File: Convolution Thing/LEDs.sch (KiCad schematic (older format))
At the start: 6 parts

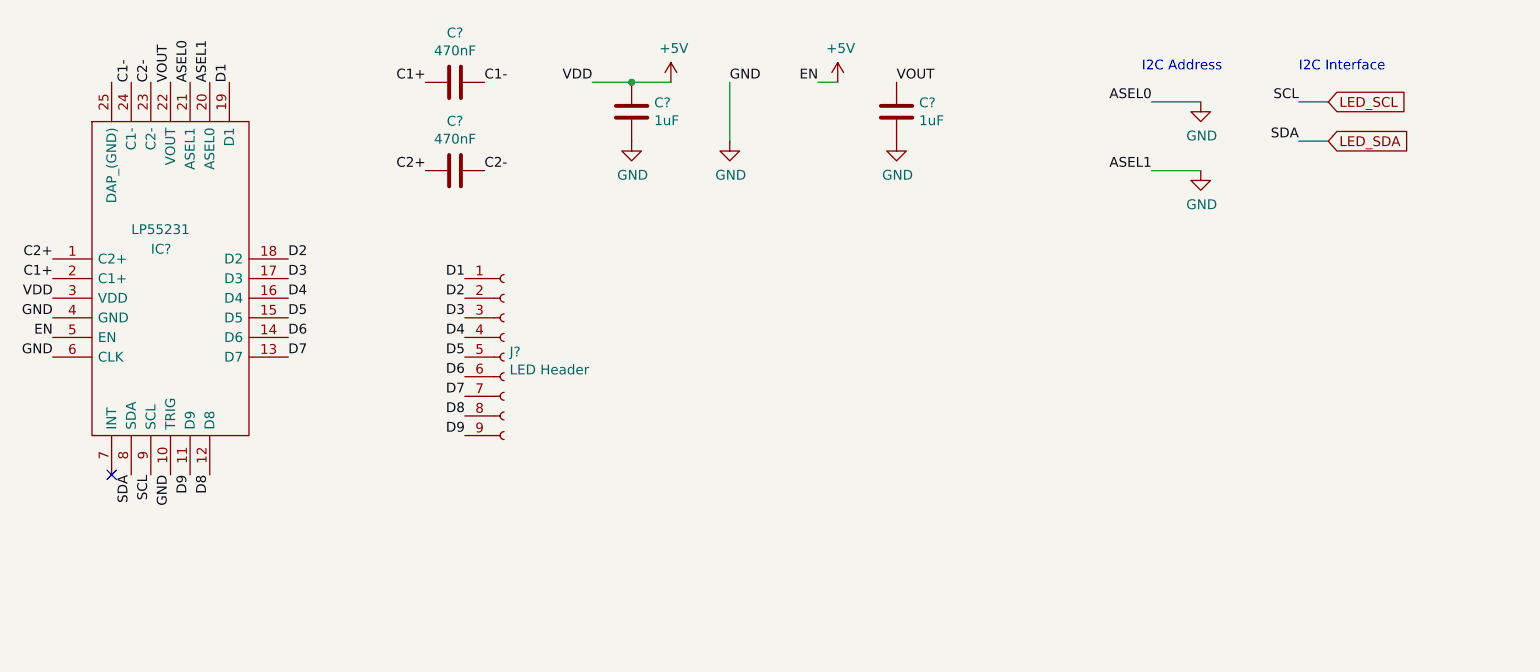
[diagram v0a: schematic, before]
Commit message: Added gate inputs and CM4 / display sockets, made CV inputs 100k, lots of smaller changes. First iteration of schematic now done.
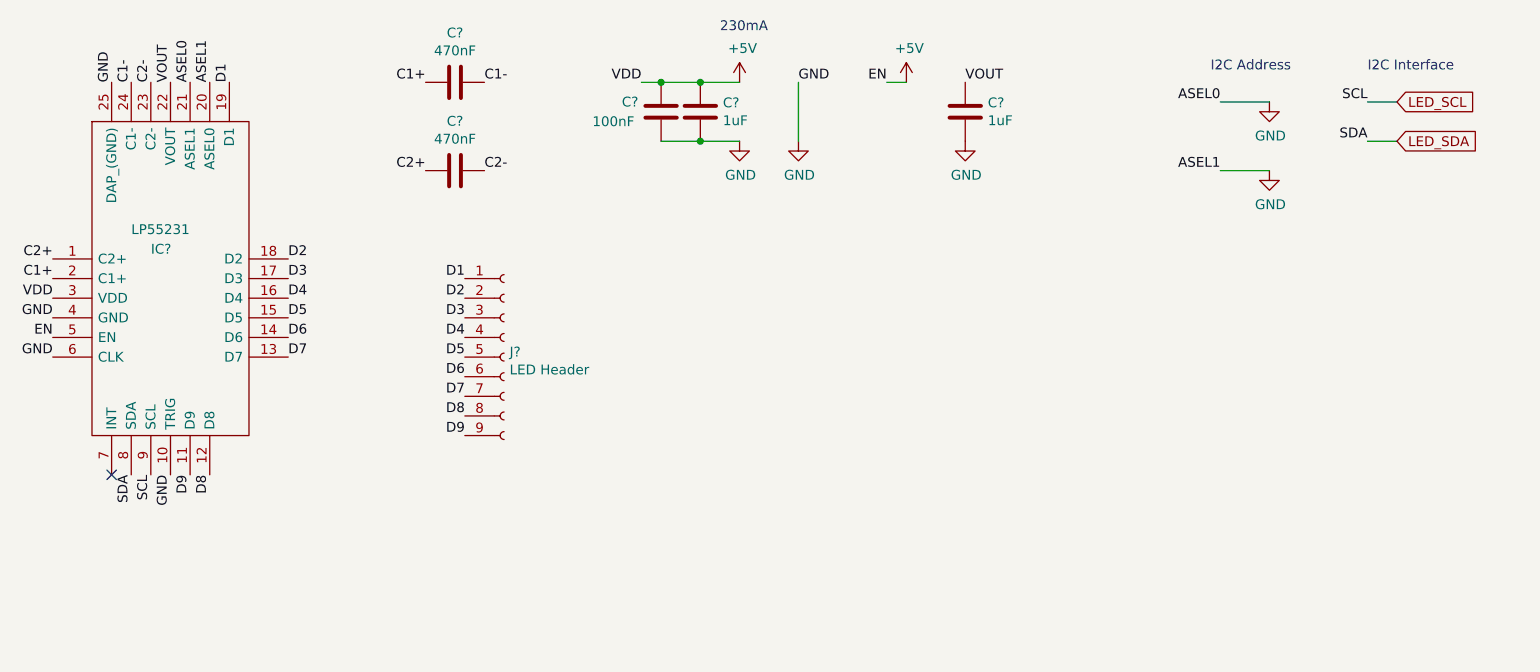
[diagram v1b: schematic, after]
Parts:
- added C?: 100nF, symbol Device:C
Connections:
- net +5V: now also C?.1
- net GND: now also IC?.25 (DAP_(GND)), C?.2
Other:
- note added: "230mA"
- moved on the sheet: C?
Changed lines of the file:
@@
 $Descr A4 11693 8268
 encoding utf-8
-Sheet 10 11
+Sheet 10 13
 Title ""
 Date ""
@@
 L power:+5V #PWR?
 U 1 1 611E96FD
-P 4350 1000
-F 0 "#PWR?" H 4350 850 50  0001 C CNN
-F 1 "+5V" H 4365 1173 50  0000 C CNN
-F 2 "" H 4350 1000 50  0001 C CNN
-F 3 "" H 4350 1000 50  0001 C CNN
-	1    4350 1000
-	1    0    0    -1
-$EndComp
-Text Label 3950 1000 2    50   ~ 0
+P 4700 1000
+F 0 "#PWR?" H 4700 850 50  0001 C CNN
+F 1 "+5V" H 4715 1173 50  0000 C CNN
+F 2 "" H 4700 1000 50  0001 C CNN
+F 3 "" H 4700 1000 50  0001 C CNN
+	1    4700 1000
+	1    0    0    -1
+$EndComp
+Text Label 4200 1000 2    50   ~ 0
 VDD
 $Comp
 L Device:C C?
 U 1 1 611EA9E5
-P 4150 1150
-F 0 "C?" H 4265 1196 50  0000 L CNN
-F 1 "1uF" H 4265 1105 50  0000 L CNN
-F 2 "" H 4188 1000 50  0001 C CNN
-F 3 "~" H 4150 1150 50  0001 C CNN
-	1    4150 1150
-	1    0    0    -1
-$EndComp
-Wire Wire Line
-	4350 1000 4150 1000
-Wire Wire Line
-	4150 1000 3950 1000
-Connection ~ 4150 1000
+P 4500 1150
+F 0 "C?" H 4615 1196 50  0000 L CNN
+F 1 "1uF" H 4615 1105 50  0000 L CNN
+F 2 "" H 4538 1000 50  0001 C CNN
+F 3 "~" H 4500 1150 50  0001 C CNN
+	1    4500 1150
+	1    0    0    -1
+$EndComp
+Wire Wire Line
+	4700 1000 4500 1000
+Wire Wire Line
+	4500 1000 4300 1000
+Connection ~ 4500 1000
 $Comp
 L power:GND #PWR?
 U 1 1 611EAE26
-P 4150 1300
-F 0 "#PWR?" H 4150 1050 50  0001 C CNN
-F 1 "GND" H 4155 1127 50  0000 C CNN
-F 2 "" H 4150 1300 50  0001 C CNN
-F 3 "" H 4150 1300 50  0001 C CNN
-	1    4150 1300
-	1    0    0    -1
-$EndComp
-Text Label 4650 1000 0    50   ~ 0
+P 4700 1300
+F 0 "#PWR?" H 4700 1050 50  0001 C CNN
+F 1 "GND" H 4705 1127 50  0000 C CNN
+F 2 "" H 4700 1300 50  0001 C CNN
+F 3 "" H 4700 1300 50  0001 C CNN
+	1    4700 1300
+	1    0    0    -1
+$EndComp
+Text Label 5000 1000 0    50   ~ 0
 GND
 $Comp
 L power:GND #PWR?
 U 1 1 611EC0F9
-P 4650 1300
-F 0 "#PWR?" H 4650 1050 50  0001 C CNN
-F 1 "GND" H 4655 1127 50  0000 C CNN
-F 2 "" H 4650 1300 50  0001 C CNN
-F 3 "" H 4650 1300 50  0001 C CNN
-	1    4650 1300
-	1    0    0    -1
-$EndComp
-Wire Wire Line
-	4650 1300 4650 1000
+P 5000 1300
+F 0 "#PWR?" H 5000 1050 50  0001 C CNN
+F 1 "GND" H 5005 1127 50  0000 C CNN
+F 2 "" H 5000 1300 50  0001 C CNN
+F 3 "" H 5000 1300 50  0001 C CNN
+	1    5000 1300
+	1    0    0    -1
+$EndComp
+Wire Wire Line
+	5000 1300 5000 1000
 Text Label 1200 2400 2    50   ~ 0
 GND
 Text Label 1200 2300 2    50   ~ 0
 EN
-Text Label 5100 1000 2    50   ~ 0
+Text Label 5450 1000 2    50   ~ 0
 EN
 $Comp
 L power:+5V #PWR?
 U 1 1 611EF36E
-P 5200 1000
-F 0 "#PWR?" H 5200 850 50  0001 C CNN
-F 1 "+5V" H 5215 1173 50  0000 C CNN
-F 2 "" H 5200 1000 50  0001 C CNN
-F 3 "" H 5200 1000 50  0001 C CNN
-	1    5200 1000
-	1    0    0    -1
-$EndComp
-Wire Wire Line
-	5200 1000 5100 1000
+P 5550 1000
+F 0 "#PWR?" H 5550 850 50  0001 C CNN
+F 1 "+5V" H 5565 1173 50  0000 C CNN
+F 2 "" H 5550 1000 50  0001 C CNN
+F 3 "" H 5550 1000 50  0001 C CNN
+	1    5550 1000
+	1    0    0    -1
+$EndComp
+Wire Wire Line
+	5550 1000 5450 1000
 NoConn ~ 1500 3000
 Text Label 1600 3000 3    50   ~ 0
@@
 Text Label 1700 3000 3    50   ~ 0
 SCL
-Text Notes 6750 950  0    50   ~ 0
+Text Notes 7100 950  0    50   ~ 0
 I2C Address
 Text Label 1900 1000 1    50   ~ 0
@@
 Text Label 2000 1000 1    50   ~ 0
 ASEL1
-Text Label 6800 1100 2    50   ~ 0
+Text Label 7150 1100 2    50   ~ 0
 ASEL0
-Text Label 6800 1450 2    50   ~ 0
+Text Label 7150 1450 2    50   ~ 0
 ASEL1
 $Comp
 L power:GND #PWR?
 U 1 1 611F4B43
-P 7050 1100
-F 0 "#PWR?" H 7050 850 50  0001 C CNN
-F 1 "GND" H 7055 927 50  0000 C CNN
-F 2 "" H 7050 1100 50  0001 C CNN
-F 3 "" H 7050 1100 50  0001 C CNN
-	1    7050 1100
-	1    0    0    -1
-$EndComp
-Wire Wire Line
-	7050 1100 6800 1100
+P 7400 1100
+F 0 "#PWR?" H 7400 850 50  0001 C CNN
+F 1 "GND" H 7405 927 50  0000 C CNN
+F 2 "" H 7400 1100 50  0001 C CNN
+F 3 "" H 7400 1100 50  0001 C CNN
+	1    7400 1100
+	1    0    0    -1
+$EndComp
+Wire Wire Line
+	7400 1100 7150 1100
 $Comp
 L power:GND #PWR?
 U 1 1 611F4F3E
-P 7050 1450
-F 0 "#PWR?" H 7050 1200 50  0001 C CNN
-F 1 "GND" H 7055 1277 50  0000 C CNN
-F 2 "" H 7050 1450 50  0001 C CNN
-F 3 "" H 7050 1450 50  0001 C CNN
-	1    7050 1450
-	1    0    0    -1
-$EndComp
-Wire Wire Line
-	7050 1450 6800 1450
-Text Notes 7550 950  0    50   ~ 0
+P 7400 1450
+F 0 "#PWR?" H 7400 1200 50  0001 C CNN
+F 1 "GND" H 7405 1277 50  0000 C CNN
+F 2 "" H 7400 1450 50  0001 C CNN
+F 3 "" H 7400 1450 50  0001 C CNN
+	1    7400 1450
+	1    0    0    -1
+$EndComp
+Wire Wire Line
+	7400 1450 7150 1450
+Text Notes 7900 950  0    50   ~ 0
 I2C Interface
-Text Label 7550 1100 2    50   ~ 0
+Text Label 7900 1100 2    50   ~ 0
 SCL
-Text Label 7550 1300 2    50   ~ 0
+Text Label 7900 1300 2    50   ~ 0
 SDA
-Text GLabel 7700 1100 2    50   Input ~ 0
+Text GLabel 8050 1100 2    50   Input ~ 0
 LED_SCL
-Text GLabel 7700 1300 2    50   Input ~ 0
+Text GLabel 8050 1300 2    50   Input ~ 0
 LED_SDA
 Wire Wire Line
-	7700 1300 7550 1300
-Wire Wire Line
-	7550 1100 7700 1100
+	8050 1300 7900 1300
+Wire Wire Line
+	7900 1100 8050 1100
 Text Label 1800 3000 3    50   ~ 0
 GND
 Text Label 1800 1000 1    50   ~ 0
 VOUT
-Text Label 5500 1000 0    50   ~ 0
+Text Label 5850 1000 0    50   ~ 0
 VOUT
 $Comp
 L Device:C C?
 U 1 1 611FB309
-P 5500 1150
-F 0 "C?" H 5615 1196 50  0000 L CNN
-F 1 "1uF" H 5615 1105 50  0000 L CNN
-F 2 "" H 5538 1000 50  0001 C CNN
-F 3 "~" H 5500 1150 50  0001 C CNN
-	1    5500 1150
+P 5850 1150
+F 0 "C?" H 5965 1196 50  0000 L CNN
+F 1 "1uF" H 5965 1105 50  0000 L CNN
+F 2 "" H 5888 1000 50  0001 C CNN
+F 3 "~" H 5850 1150 50  0001 C CNN
+	1    5850 1150
 	1    0    0    -1
 $EndComp
@@
 L power:GND #PWR?
 U 1 1 611FB5AF
-P 5500 1300
-F 0 "#PWR?" H 5500 1050 50  0001 C CNN
-F 1 "GND" H 5505 1127 50  0000 C CNN
-F 2 "" H 5500 1300 50  0001 C CNN
-F 3 "" H 5500 1300 50  0001 C CNN
-	1    5500 1300
+P 5850 1300
+F 0 "#PWR?" H 5850 1050 50  0001 C CNN
+F 1 "GND" H 5855 1127 50  0000 C CNN
+F 2 "" H 5850 1300 50  0001 C CNN
+F 3 "" H 5850 1300 50  0001 C CNN
+	1    5850 1300
 	1    0    0    -1
 $EndComp
@@
 Text Label 3300 2800 2    50   ~ 0
 D9
+Text Label 1500 1000 1    50   ~ 0
+GND
+Text Notes 4600 750  0    50   ~ 0
+230mA
+$Comp
+L Device:C C?
+U 1 1 612CC466
+P 4300 1150
+F 0 "C?" H 4100 1200 50  0000 L CNN
+F 1 "100nF" H 3950 1100 50  0000 L CNN
+F 2 "" H 4338 1000 50  0001 C CNN
+F 3 "~" H 4300 1150 50  0001 C CNN
+	1    4300 1150
+	1    0    0    -1
+$EndComp
+Wire Wire Line
+	4200 1000 4300 1000
+Connection ~ 4300 1000
+Wire Wire Line
+	4300 1300 4500 1300
+Wire Wire Line
+	4500 1300 4700 1300
+Connection ~ 4500 1300
 $EndSCHEMATC

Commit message: Fix some issues, add component references
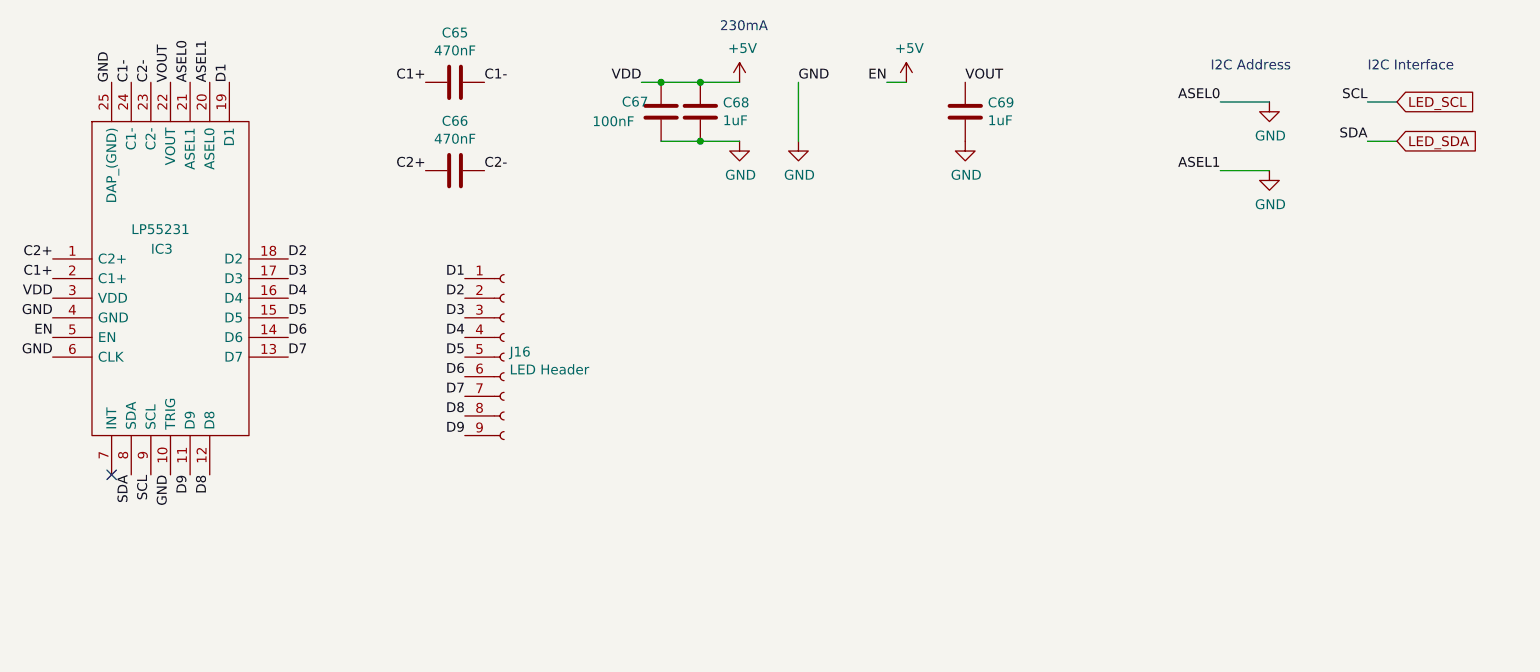
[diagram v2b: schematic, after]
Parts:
- gave numbers to parts that had none: 7
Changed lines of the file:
@@
 $EndDescr
 $Comp
-L SamacSys:LP55231SQE_NOPB IC?
+L SamacSys:LP55231SQE_NOPB IC3
 U 1 1 611DF4B0
 P 1200 1900
-F 0 "IC?" H 1700 1950 50  0000 L CNN
+F 0 "IC3" H 1700 1950 50  0000 L CNN
 F 1 "LP55231" H 1600 2050 50  0000 L CNN
 F 2 "QFN50P400X400X80-25N" H 2250 2600 50  0001 L CNN
@@
 C1+
 $Comp
-L Device:C C?
+L Device:C C65
 U 1 1 611E401F
 P 3250 1000
-F 0 "C?" V 2998 1000 50  0000 C CNN
+F 0 "C65" V 2998 1000 50  0000 C CNN
 F 1 "470nF" V 3089 1000 50  0000 C CNN
 F 2 "" H 3288 850 50  0001 C CNN
@@
 C2+
 $Comp
-L Device:C C?
+L Device:C C66
 U 1 1 611E6D48
 P 3250 1450
-F 0 "C?" V 2998 1450 50  0000 C CNN
+F 0 "C66" V 2998 1450 50  0000 C CNN
 F 1 "470nF" V 3089 1450 50  0000 C CNN
 F 2 "" H 3288 1300 50  0001 C CNN
@@
 C2-
 $Comp
-L power:+5V #PWR?
+L power:+5V #PWR0119
 U 1 1 611E96FD
 P 4700 1000
-F 0 "#PWR?" H 4700 850 50  0001 C CNN
+F 0 "#PWR0119" H 4700 850 50  0001 C CNN
 F 1 "+5V" H 4715 1173 50  0000 C CNN
 F 2 "" H 4700 1000 50  0001 C CNN
@@
 VDD
 $Comp
-L Device:C C?
+L Device:C C68
 U 1 1 611EA9E5
 P 4500 1150
-F 0 "C?" H 4615 1196 50  0000 L CNN
+F 0 "C68" H 4615 1196 50  0000 L CNN
 F 1 "1uF" H 4615 1105 50  0000 L CNN
 F 2 "" H 4538 1000 50  0001 C CNN
@@
 Connection ~ 4500 1000
 $Comp
-L power:GND #PWR?
+L power:GND #PWR0120
 U 1 1 611EAE26
 P 4700 1300
-F 0 "#PWR?" H 4700 1050 50  0001 C CNN
+F 0 "#PWR0120" H 4700 1050 50  0001 C CNN
 F 1 "GND" H 4705 1127 50  0000 C CNN
 F 2 "" H 4700 1300 50  0001 C CNN
@@
 GND
 $Comp
-L power:GND #PWR?
+L power:GND #PWR0121
 U 1 1 611EC0F9
 P 5000 1300
-F 0 "#PWR?" H 5000 1050 50  0001 C CNN
+F 0 "#PWR0121" H 5000 1050 50  0001 C CNN
 F 1 "GND" H 5005 1127 50  0000 C CNN
 F 2 "" H 5000 1300 50  0001 C CNN
@@
 EN
 $Comp
-L power:+5V #PWR?
+L power:+5V #PWR0122
 U 1 1 611EF36E
 P 5550 1000
-F 0 "#PWR?" H 5550 850 50  0001 C CNN
+F 0 "#PWR0122" H 5550 850 50  0001 C CNN
 F 1 "+5V" H 5565 1173 50  0000 C CNN
 F 2 "" H 5550 1000 50  0001 C CNN
@@
 ASEL1
 $Comp
-L power:GND #PWR?
+L power:GND #PWR0124
 U 1 1 611F4B43
 P 7400 1100
-F 0 "#PWR?" H 7400 850 50  0001 C CNN
+F 0 "#PWR0124" H 7400 850 50  0001 C CNN
 F 1 "GND" H 7405 927 50  0000 C CNN
 F 2 "" H 7400 1100 50  0001 C CNN
@@
 	7400 1100 7150 1100
 $Comp
-L power:GND #PWR?
+L power:GND #PWR0125
 U 1 1 611F4F3E
 P 7400 1450
-F 0 "#PWR?" H 7400 1200 50  0001 C CNN
+F 0 "#PWR0125" H 7400 1200 50  0001 C CNN
 F 1 "GND" H 7405 1277 50  0000 C CNN
 F 2 "" H 7400 1450 50  0001 C CNN
@@
 VOUT
 $Comp
-L Device:C C?
+L Device:C C69
 U 1 1 611FB309
 P 5850 1150
-F 0 "C?" H 5965 1196 50  0000 L CNN
+F 0 "C69" H 5965 1196 50  0000 L CNN
 F 1 "1uF" H 5965 1105 50  0000 L CNN
 F 2 "" H 5888 1000 50  0001 C CNN
@@
 $EndComp
 $Comp
-L power:GND #PWR?
+L power:GND #PWR0123
 U 1 1 611FB5AF
 P 5850 1300
-F 0 "#PWR?" H 5850 1050 50  0001 C CNN
+F 0 "#PWR0123" H 5850 1050 50  0001 C CNN
 F 1 "GND" H 5855 1127 50  0000 C CNN
 F 2 "" H 5850 1300 50  0001 C CNN
@@
 D9
 $Comp
-L Connector:Conn_01x09_Female J?
+L Connector:Conn_01x09_Female J16
 U 1 1 611FEF8C
 P 3500 2400
-F 0 "J?" H 3528 2426 50  0000 L CNN
+F 0 "J16" H 3528 2426 50  0000 L CNN
 F 1 "LED Header" H 3528 2335 50  0000 L CNN
 F 2 "" H 3500 2400 50  0001 C CNN
@@
 230mA
 $Comp
-L Device:C C?
+L Device:C C67
 U 1 1 612CC466
 P 4300 1150
-F 0 "C?" H 4100 1200 50  0000 L CNN
+F 0 "C67" H 4100 1200 50  0000 L CNN
 F 1 "100nF" H 3950 1100 50  0000 L CNN
 F 2 "" H 4338 1000 50  0001 C CNN

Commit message: Started footprint assignment
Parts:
- IC3: footprint QFN50P400X400X80-25N -> SamacSys:QFN50P400X400X80-25N
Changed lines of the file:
@@
 F 0 "IC3" H 1700 1950 50  0000 L CNN
 F 1 "LP55231" H 1600 2050 50  0000 L CNN
-F 2 "QFN50P400X400X80-25N" H 2250 2600 50  0001 L CNN
+F 2 "SamacSys:QFN50P400X400X80-25N" H 2250 2600 50  0001 L CNN
 F 3 "" H 2250 2500 50  0001 L CNN
 F 4 "9 Channel RGB / White LED Driver with Internal Program Memory and Integrated Charge Pump - WQFN" H 2250 2400 50  0001 L CNN "Description"

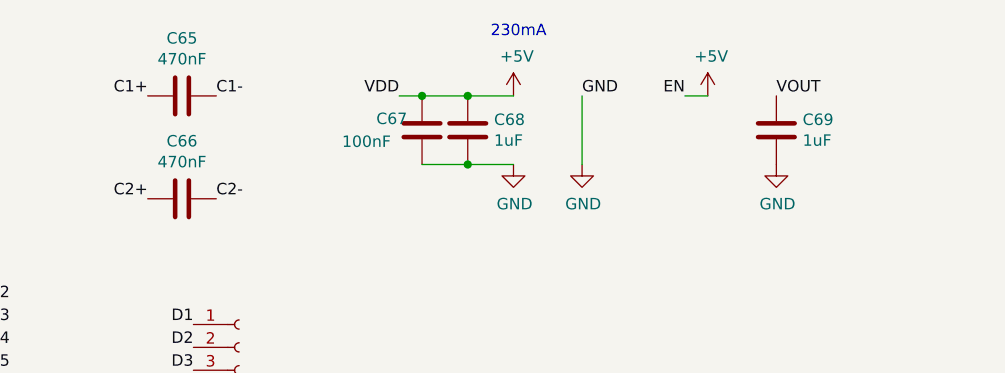
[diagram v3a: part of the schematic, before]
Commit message: Assign all footprints
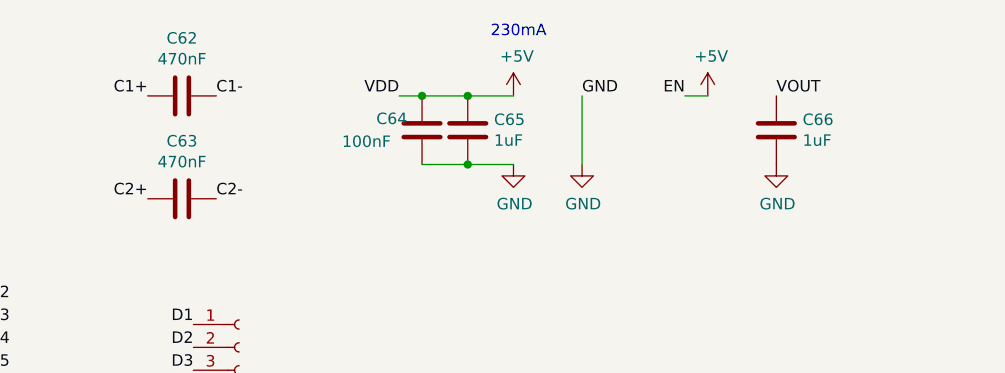
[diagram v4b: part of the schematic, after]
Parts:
- C62: renamed from C65; footprint (none) -> Capacitor_SMD:C_0805_2012Metric
- C63: renamed from C66; footprint (none) -> Capacitor_SMD:C_0805_2012Metric
- C64: renamed from C67; footprint (none) -> Capacitor_SMD:C_0805_2012Metric
- C65: renamed from C68; footprint (none) -> Capacitor_SMD:C_0805_2012Metric
- C66: renamed from C69; footprint (none) -> Capacitor_SMD:C_0805_2012Metric
- J16: footprint (none) -> Connector_PinHeader_2.54mm:PinHeader_1x09_P2.54mm_Vertical
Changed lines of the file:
@@
 C1+
 $Comp
-L Device:C C65
+L Device:C C62
 U 1 1 611E401F
 P 3250 1000
-F 0 "C65" V 2998 1000 50  0000 C CNN
+F 0 "C62" V 2998 1000 50  0000 C CNN
 F 1 "470nF" V 3089 1000 50  0000 C CNN
-F 2 "" H 3288 850 50  0001 C CNN
+F 2 "Capacitor_SMD:C_0805_2012Metric" H 3288 850 50  0001 C CNN
 F 3 "~" H 3250 1000 50  0001 C CNN
 	1    3250 1000
@@
 C2+
 $Comp
-L Device:C C66
+L Device:C C63
 U 1 1 611E6D48
 P 3250 1450
-F 0 "C66" V 2998 1450 50  0000 C CNN
+F 0 "C63" V 2998 1450 50  0000 C CNN
 F 1 "470nF" V 3089 1450 50  0000 C CNN
-F 2 "" H 3288 1300 50  0001 C CNN
+F 2 "Capacitor_SMD:C_0805_2012Metric" H 3288 1300 50  0001 C CNN
 F 3 "~" H 3250 1450 50  0001 C CNN
 	1    3250 1450
@@
 C2-
 $Comp
-L power:+5V #PWR0119
+L power:+5V #PWR0112
 U 1 1 611E96FD
 P 4700 1000
-F 0 "#PWR0119" H 4700 850 50  0001 C CNN
+F 0 "#PWR0112" H 4700 850 50  0001 C CNN
 F 1 "+5V" H 4715 1173 50  0000 C CNN
 F 2 "" H 4700 1000 50  0001 C CNN
@@
 VDD
 $Comp
-L Device:C C68
+L Device:C C65
 U 1 1 611EA9E5
 P 4500 1150
-F 0 "C68" H 4615 1196 50  0000 L CNN
+F 0 "C65" H 4615 1196 50  0000 L CNN
 F 1 "1uF" H 4615 1105 50  0000 L CNN
-F 2 "" H 4538 1000 50  0001 C CNN
+F 2 "Capacitor_SMD:C_0805_2012Metric" H 4538 1000 50  0001 C CNN
 F 3 "~" H 4500 1150 50  0001 C CNN
 	1    4500 1150
@@
 Connection ~ 4500 1000
 $Comp
-L power:GND #PWR0120
+L power:GND #PWR0113
 U 1 1 611EAE26
 P 4700 1300
-F 0 "#PWR0120" H 4700 1050 50  0001 C CNN
+F 0 "#PWR0113" H 4700 1050 50  0001 C CNN
 F 1 "GND" H 4705 1127 50  0000 C CNN
 F 2 "" H 4700 1300 50  0001 C CNN
@@
 GND
 $Comp
-L power:GND #PWR0121
+L power:GND #PWR0114
 U 1 1 611EC0F9
 P 5000 1300
-F 0 "#PWR0121" H 5000 1050 50  0001 C CNN
+F 0 "#PWR0114" H 5000 1050 50  0001 C CNN
 F 1 "GND" H 5005 1127 50  0000 C CNN
 F 2 "" H 5000 1300 50  0001 C CNN
@@
 EN
 $Comp
-L power:+5V #PWR0122
+L power:+5V #PWR0115
 U 1 1 611EF36E
 P 5550 1000
-F 0 "#PWR0122" H 5550 850 50  0001 C CNN
+F 0 "#PWR0115" H 5550 850 50  0001 C CNN
 F 1 "+5V" H 5565 1173 50  0000 C CNN
 F 2 "" H 5550 1000 50  0001 C CNN
@@
 ASEL1
 $Comp
-L power:GND #PWR0124
+L power:GND #PWR0117
 U 1 1 611F4B43
 P 7400 1100
-F 0 "#PWR0124" H 7400 850 50  0001 C CNN
+F 0 "#PWR0117" H 7400 850 50  0001 C CNN
 F 1 "GND" H 7405 927 50  0000 C CNN
 F 2 "" H 7400 1100 50  0001 C CNN
@@
 	7400 1100 7150 1100
 $Comp
-L power:GND #PWR0125
+L power:GND #PWR0118
 U 1 1 611F4F3E
 P 7400 1450
-F 0 "#PWR0125" H 7400 1200 50  0001 C CNN
+F 0 "#PWR0118" H 7400 1200 50  0001 C CNN
 F 1 "GND" H 7405 1277 50  0000 C CNN
 F 2 "" H 7400 1450 50  0001 C CNN
@@
 VOUT
 $Comp
-L Device:C C69
+L Device:C C66
 U 1 1 611FB309
 P 5850 1150
-F 0 "C69" H 5965 1196 50  0000 L CNN
+F 0 "C66" H 5965 1196 50  0000 L CNN
 F 1 "1uF" H 5965 1105 50  0000 L CNN
-F 2 "" H 5888 1000 50  0001 C CNN
+F 2 "Capacitor_SMD:C_0805_2012Metric" H 5888 1000 50  0001 C CNN
 F 3 "~" H 5850 1150 50  0001 C CNN
 	1    5850 1150
@@
 $EndComp
 $Comp
-L power:GND #PWR0123
+L power:GND #PWR0116
 U 1 1 611FB5AF
 P 5850 1300
-F 0 "#PWR0123" H 5850 1050 50  0001 C CNN
+F 0 "#PWR0116" H 5850 1050 50  0001 C CNN
 F 1 "GND" H 5855 1127 50  0000 C CNN
 F 2 "" H 5850 1300 50  0001 C CNN
@@
 F 0 "J16" H 3528 2426 50  0000 L CNN
 F 1 "LED Header" H 3528 2335 50  0000 L CNN
-F 2 "" H 3500 2400 50  0001 C CNN
+F 2 "Connector_PinHeader_2.54mm:PinHeader_1x09_P2.54mm_Vertical" H 3500 2400 50  0001 C CNN
 F 3 "~" H 3500 2400 50  0001 C CNN
 	1    3500 2400
@@
 230mA
 $Comp
-L Device:C C67
+L Device:C C64
 U 1 1 612CC466
 P 4300 1150
-F 0 "C67" H 4100 1200 50  0000 L CNN
+F 0 "C64" H 4100 1200 50  0000 L CNN
 F 1 "100nF" H 3950 1100 50  0000 L CNN
-F 2 "" H 4338 1000 50  0001 C CNN
+F 2 "Capacitor_SMD:C_0805_2012Metric" H 4338 1000 50  0001 C CNN
 F 3 "~" H 4300 1150 50  0001 C CNN
 	1    4300 1150
